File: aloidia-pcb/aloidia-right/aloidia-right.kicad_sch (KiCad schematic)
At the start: 220 parts, among them J1 SWD_02x05_1.27mm, J10 Pin headers 2.54mm 01x02, J11 USB4105-GF-A-120, J12 SM08B-SRSS-TB(LF)(SN), J2 SM08B-SRSS-TB(LF)(SN), J3 SM06B-SRSS-TB, J4 SM03B-SRSS-TB(LF)(SN), J5 Picoblade 0532614002, J6 Pin headers 2.54mm 01x03, J7 USB4105-GF-A-120, J9 SM04B-SRSS-TB(LF)(SN), Q1 PJA3404, Q2 DMG9926UDM, Q3 Si2371EDS, Q4 Si2371EDS, Q5 PJA3404, SW1 SSSS213100, SW100 SW_Push, SW101 SW_Push, SW102 SW_Push, SW103 SW_Push, SW104 SW_Push, SW105 SW_Push, SW107 SW_Push, SW108 MX_EC11, SW110 SW_Push, SW111 SW_Push, SW112 SW_Push, SW113 SW_Push, SW114 SW_Push, SW115 SW_Push, SW116 SW_Push, SW117 SW_Push, SW118 SW_Push, SW120 SW_Push, SW121 SW_Push, SW122 SW_Push, SW123 SW_Push, SW124 SW_Push, SW125 SW_Push, SW127 SW_Push, SW128 SW_Push, SW130 SW_Push, SW131 SW_Push, SW132 SW_Push, SW133 SW_Push, SW134 SW_Push, SW135 SW_Push, SW137 SW_Push, SW138 SW_Push, SW140 MX_EVQWGD001, SW141 SW_Push, SW142 SW_Push, SW143 SW_Push, SW144 SW_Push, SW145 SW_Push, SW147 SW_Push, SW148 SW_Push, SW2 EG6201, SW241 SW_Push, U1 MAX17048, U2 MDBT50Q-1MV2, U3 MCP1812AT-033/TT, U4 DMN2004DMK-7, U5 BQ24075RGT, U6 AP9101CK6-ANTRG1, U7 STS234050UL30, U8 BQ25504, U9 LTC4359-MS8, Y1 32.768kHz

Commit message: Replaced usb by THT and reverse mounted
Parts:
- H1, H2, H3, H4: value 3.2mm_M3 -> 2.2mm_M2; footprint MountingHole:MountingHole_3.2mm_M3_Pad -> MountingHole:MountingHole_2.2mm_M2_Pad
- J11, J7: value USB4105-GF-A-120 -> USB4085-GF-A; footprint Connector_USB:USB_C_Receptacle_HRO_TYPE-C-31-M-12 -> Connector_USB:USB_C_Receptacle_GCT_USB4085; Digikey ref (none) -> 2073-USB4085-GF-ACT-ND; Manufacturer ref USB4105-GF-A-120 -> USB4085-GF-A; Mouser ref 640-USB4105-GF-A-120 -> (none)
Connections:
- net +3.3V: now also J12.7 (Pin_7), J2.7 (Pin_7); no longer J12.2 (Pin_2), J2.2 (Pin_2)
- net +BATT_PULLUP: now also SW1.3 (C); no longer SW1.1 (A)
- net BUSY: now also J12.1 (Pin_1), J2.1 (Pin_1), U2.23 (TRACECLK/P0.07); no longer J12.8 (Pin_8), J2.8 (Pin_8), U2.16 (P0.27)
- net CS: now also J12.4 (Pin_4), J2.4 (Pin_4), U2.20 (P0.04/AIN2); no longer J12.5 (Pin_5), J2.5 (Pin_5), U2.21 (P0.05/AIN3)
- net DC: now also J12.3 (Pin_3), J2.3 (Pin_3), U2.21 (P0.05/AIN3); no longer J12.6 (Pin_6), J2.6 (Pin_6), U2.20 (P0.04/AIN2)
- net DIN: now also J12.6 (Pin_6), J2.6 (Pin_6), U2.16 (P0.27); no longer J12.3 (Pin_3), J2.3 (Pin_3), U2.23 (TRACECLK/P0.07)
- net GND: now also J12.8 (Pin_8), J2.8 (Pin_8), SW1.1 (A); no longer J12.1 (Pin_1), J2.1 (Pin_1), SW1.3 (C)
- net RST: now also J12.2 (Pin_2), J2.2 (Pin_2), U2.22 (P0.06); no longer J12.7 (Pin_7), J2.7 (Pin_7), U2.19 (P0.26)
- net SCK: now also J12.5 (Pin_5), J2.5 (Pin_5), U2.19 (P0.26); no longer J12.4 (Pin_4), J2.4 (Pin_4), U2.22 (P0.06)

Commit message: Added graphic elements
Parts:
- removed TP32: GND, 0_various:TestPoint, symbol Connector:TestPoint
- added G1: Aloidia_Logo, 0_various:aloidia_logo, symbol 0_various:Aloidia_Logo
- JP1: value REV_PROT_DISABLE -> OVCH_PROT_DISABLE
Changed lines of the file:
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@@
     (stroke (width 0) (type default) (color 0 0 0 0))
   )
-  (wire (pts (xy 443.23 400.05) (xy 450.85 400.05))
-    (stroke (width 0) (type default) (color 0 0 0 0))
-  )
   (wire (pts (xy 295.91 347.345) (xy 292.735 347.345))
     (stroke (width 0) (type default) (color 0 0 0 0))
@@
     (pin "S1")
   )
-  (symbol (lib_id "Connector:TestPoint") (at 443.23 400.05 90) (unit 1)
-    (in_bom no) (on_board yes)
-    (property "Reference" "TP32" (id 0) (at 432.435 400.05 90)
-      (effects (font (size 1.27 1.27)) (justify right))
-    )
-    (property "Value" "GND" (id 1) (at 429.26 400.05 90)
-      (effects (font (size 1.27 1.27)) (justify left))
-    )
-    (property "Footprint" "0_various:TestPoint" (id 2) (at 443.23 394.97 0)
-      (effects (font (size 1.27 1.27)) hide)
-    )
-    (property "Datasheet" "~" (id 3) (at 443.23 394.97 0)
-      (effects (font (size 1.27 1.27)) hide)
-    )
-    (pin "1")
-  )
   (symbol (lib_id "Switch:SW_Push") (at 322.58 83.185 0) (unit 1)
     (in_bom yes) (on_board yes) (fields_autoplaced)
@@
     (in_bom no) (on_board yes) (fields_autoplaced)
     (property "Reference" "JP1" (id 0) (at 302.26 275.59 0))
-    (property "Value" "REV_PROT_DISABLE" (id 1) (at 302.26 278.13 0))
+    (property "Value" "OVCH_PROT_DISABLE" (id 1) (at 302.26 278.13 0))
     (property "Footprint" "Jumper:SolderJumper-2_P1.3mm_Open_TrianglePad1.0x1.5mm" (id 2) (at 302.26 281.94 0)
       (effects (font (size 1.27 1.27)) hide)
@@
     (pin "2")
   )
+  (symbol (lib_id "0_various:Aloidia_Logo") (at 411.48 127.635 0) (unit 1)
+    (in_bom yes) (on_board yes) (fields_autoplaced)
+    (property "Reference" "G1" (id 0) (at 458.47 130.3235 0)
+      (effects (font (size 1.27 1.27)) (justify left))
+    )
+    (property "Value" "Aloidia_Logo" (id 1) (at 458.47 132.8635 0)
+      (effects (font (size 1.27 1.27)) (justify left))
+    )
+    (property "Footprint" "0_various:aloidia_logo" (id 2) (at 411.48 127.635 0)
+      (effects (font (size 1.27 1.27)) hide)
+    )
+    (property "Datasheet" "" (id 3) (at 411.48 127.635 0)
+      (effects (font (size 1.27 1.27)) hide)
+    )
+  )
   (symbol (lib_id "power:GND") (at 450.85 387.35 90) (unit 1)
     (in_bom yes) (on_board yes) (fields_autoplaced)
@@
     (pin "1")
   )
-  (symbol (lib_id "power:GND") (at 450.85 400.05 90) (unit 1)
-    (in_bom yes) (on_board yes)
-    (property "Reference" "#PWR063" (id 0) (at 457.2 400.05 0)
-      (effects (font (size 1.27 1.27)) hide)
-    )
-    (property "Value" "GND" (id 1) (at 454.025 400.0499 90)
-      (effects (font (size 1.27 1.27)) (justify right))
-    )
-    (property "Footprint" "" (id 2) (at 450.85 400.05 0)
-      (effects (font (size 1.27 1.27)) hide)
-    )
-    (property "Datasheet" "" (id 3) (at 450.85 400.05 0)
-      (effects (font (size 1.27 1.27)) hide)
-    )
-    (pin "1")
-  )
   (symbol (lib_id "Switch:SW_Push") (at 281.94 67.945 0) (unit 1)
     (in_bom yes) (on_board yes) (fields_autoplaced)
@@
       (reference "#PWR062") (unit 1) (value "GND") (footprint "")
     )
-    (path "/c9d31fd6-aa01-406e-afdc-1558e84b869f"
-      (reference "#PWR063") (unit 1) (value "GND") (footprint "")
-    )
     (path "/78c878db-eacc-4620-9cf2-799bfe2e6fff"
       (reference "#PWR064") (unit 1) (value "GND") (footprint "")
@@
       (reference "FB2") (unit 1) (value "MH2029-600Y") (footprint "Inductor_SMD:L_0805_2012Metric")
     )
+    (path "/ac0c0afb-23fc-4351-9d6b-55621237b424"
+      (reference "G1") (unit 1) (value "Aloidia_Logo") (footprint "0_various:aloidia_logo")
+    )
     (path "/584e654a-fe43-413a-84de-c3889938e191"
       (reference "H1") (unit 1) (value "2.2mm_M2") (footprint "MountingHole:MountingHole_2.2mm_M2_Pad")
@@
     )
     (path "/6cdd3c99-5837-4b31-8029-55819d65dd32"
-      (reference "JP1") (unit 1) (value "REV_PROT_DISABLE") (footprint "Jumper:SolderJumper-2_P1.3mm_Open_TrianglePad1.0x1.5mm")
+      (reference "JP1") (unit 1) (value "OVCH_PROT_DISABLE") (footprint "Jumper:SolderJumper-2_P1.3mm_Open_TrianglePad1.0x1.5mm")
     )
     (path "/908ca2a8-06e2-4247-b412-abb08a4f25fd"
@@
       (reference "TP31") (unit 1) (value "GND") (footprint "0_various:TestPoint")
     )
-    (path "/2f08ede4-1614-4d3a-8e9d-e051c974565a"
-      (reference "TP32") (unit 1) (value "GND") (footprint "0_various:TestPoint")
-    )
     (path "/9ef2aece-16db-4a17-8d42-e827f124674f"

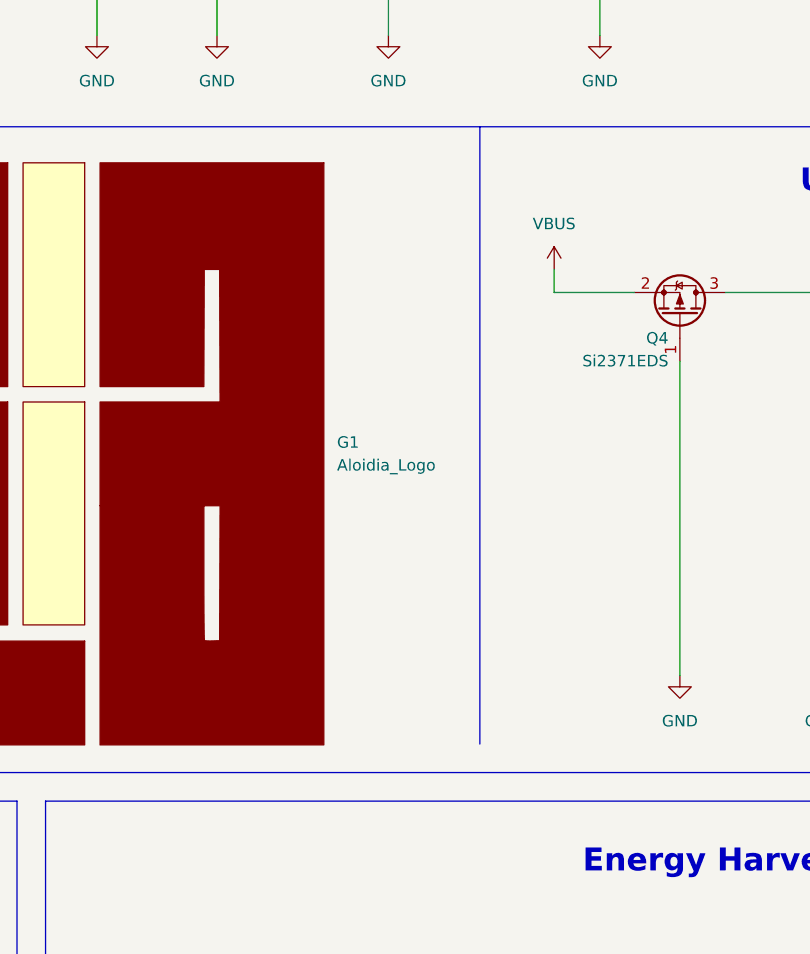
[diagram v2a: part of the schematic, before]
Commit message: Added left/right text on schematic
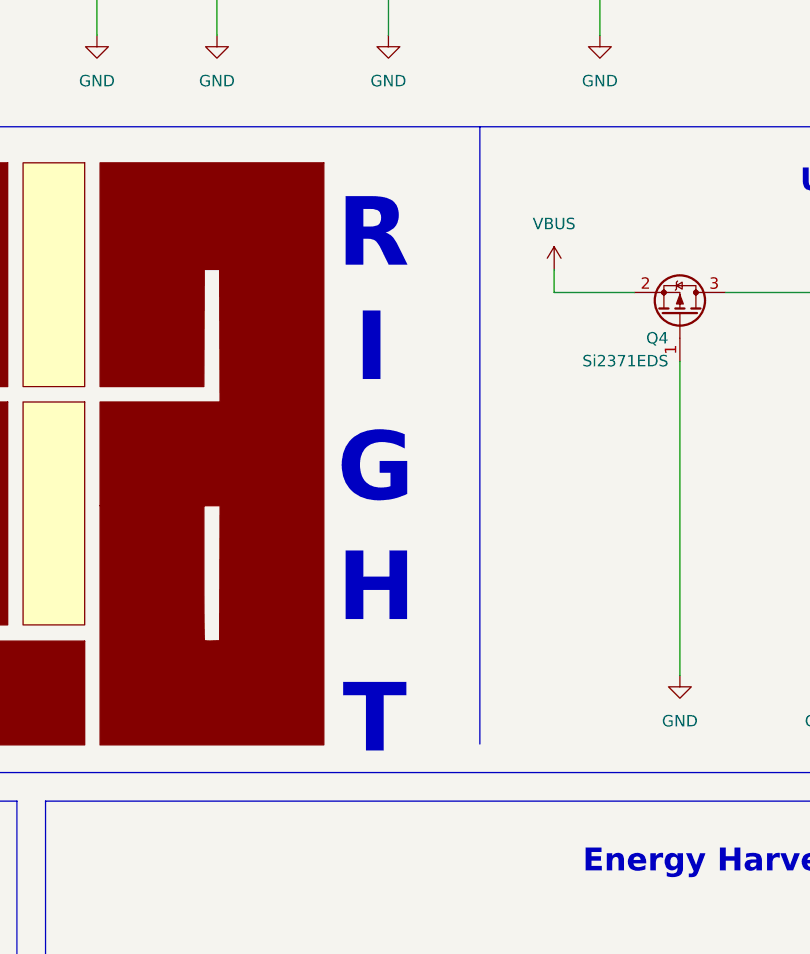
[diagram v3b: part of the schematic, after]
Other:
- note added: "G"
- note added: "H"
- note added: "I"
- note added: "R"
- note added: "T"
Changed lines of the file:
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@@
     (effects (font (size 1.27 1.27)) (justify left bottom))
   )
+  (text "H" (at 458.47 151.13 0)
+    (effects (font (size 7.62 7.62) (thickness 2.54) bold) (justify left bottom))
+  )
   (text "Power Flags" (at 514.35 328.93 0)
     (effects (font (size 2.54 2.54) (thickness 0.508) bold) (justify left bottom))
@@
     (effects (font (size 2.54 2.54) (thickness 0.508) bold) (justify left bottom))
   )
+  (text "I" (at 460.375 124.46 0)
+    (effects (font (size 7.62 7.62) (thickness 2.54) bold) (justify left bottom))
+  )
   (text "Reset" (at 109.22 193.675 0)
     (effects (font (size 2.54 2.54) (thickness 0.508) bold) (justify left bottom))
@@
     (effects (font (size 2.54 2.54) (thickness 0.508) bold) (justify left bottom))
   )
+  (text "G" (at 458.47 137.795 0)
+    (effects (font (size 7.62 7.62) (thickness 2.54) bold) (justify left bottom))
+  )
+  (text "T" (at 459.105 165.735 0)
+    (effects (font (size 7.62 7.62) (thickness 2.54) bold) (justify left bottom))
+  )
   (text "Battery Connectors" (at 374.015 243.84 0)
     (effects (font (size 2.54 2.54) (thickness 0.508) bold) (justify left bottom))
@@
     (effects (font (size 1.27 1.27)) (justify left bottom))
   )
+  (text "R" (at 458.47 111.76 0)
+    (effects (font (size 7.62 7.62) (thickness 2.54) bold) (justify left bottom))
+  )
   (text "Status/Charge RGB LED" (at 141.605 328.93 0)
     (effects (font (size 2.54 2.54) (thickness 0.508) bold) (justify left bottom))
@@
   )
   (symbol (lib_id "0_various:Aloidia_Logo") (at 411.48 127.635 0) (unit 1)
-    (in_bom yes) (on_board yes) (fields_autoplaced)
+    (in_bom yes) (on_board yes)
     (property "Reference" "G1" (id 0) (at 458.47 130.3235 0)
-      (effects (font (size 1.27 1.27)) (justify left))
+      (effects (font (size 1.27 1.27)) (justify left) hide)
     )
     (property "Value" "Aloidia_Logo" (id 1) (at 458.47 132.8635 0)
-      (effects (font (size 1.27 1.27)) (justify left))
+      (effects (font (size 1.27 1.27)) (justify left) hide)
     )
     (property "Footprint" "0_various:aloidia_logo" (id 2) (at 411.48 127.635 0)
